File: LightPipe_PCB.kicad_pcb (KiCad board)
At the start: 4 copper layers, 38.8 x 38.8 mm, 14 parts, among them M1 2.2mm_M2, M2 2.2mm_M2, X1 KLB-4, X2 KLB-4, X3 XT30, X4.1 Cable-0.7mm, X4.2 Cable-0.7mm, X5.1 Cable-1.5mm, X5.2 Cable-1.5mm

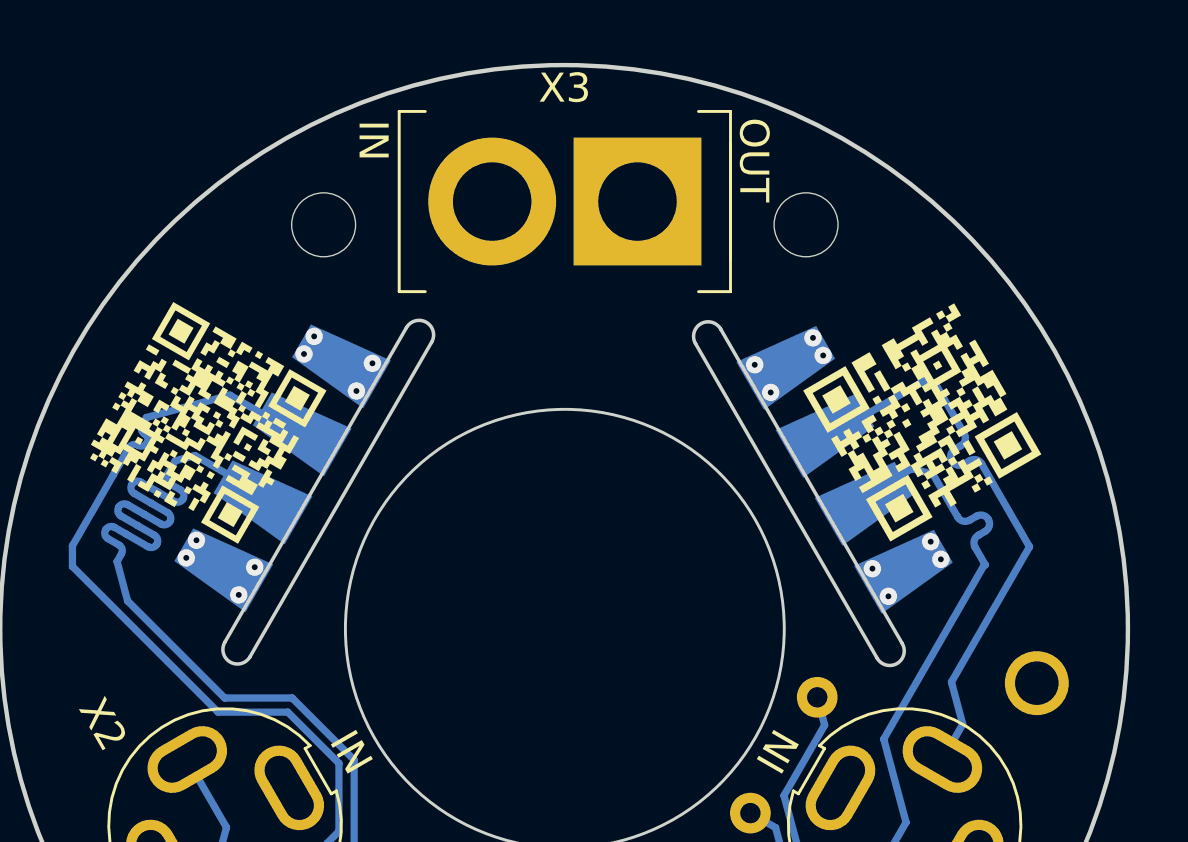
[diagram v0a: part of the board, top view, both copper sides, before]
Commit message: [clean] Optimized schematic to be easy readable as input PCB | changed 3D bodys in PCB to Input PCB positions | update date, company, project name and QR-code in schematic and board
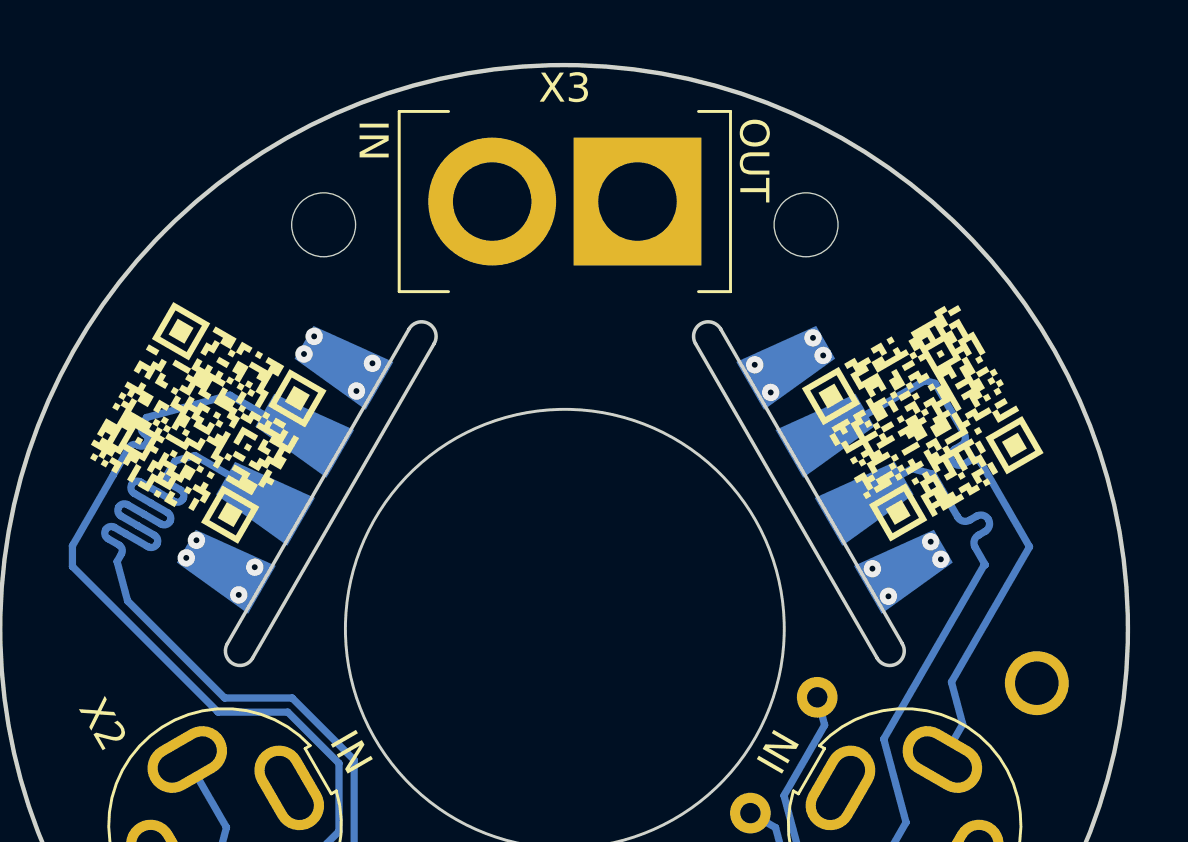
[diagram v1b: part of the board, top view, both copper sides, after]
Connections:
- LD1 pad 2: /clk2 -> /clk1
- LD1 pad 3: /d2 -> /d1
- LD2 pad 2: /clk1 -> /clk2
- LD2 pad 3: /d1 -> /d2
- LD3 pad 2: /clk1 -> /clk2
- LD3 pad 3: /d1 -> /d2
- X1 pad 1: /clk2 -> /clk1
- X1 pad 2: /d2 -> /d1
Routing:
- net /clk2: track 20.0 -> 45.5 mm
- net /clk1: track 45.5 -> 20.0 mm
- net /d2: track 20.0 -> 45.4 mm
- net /d1: track 45.4 -> 20.0 mm

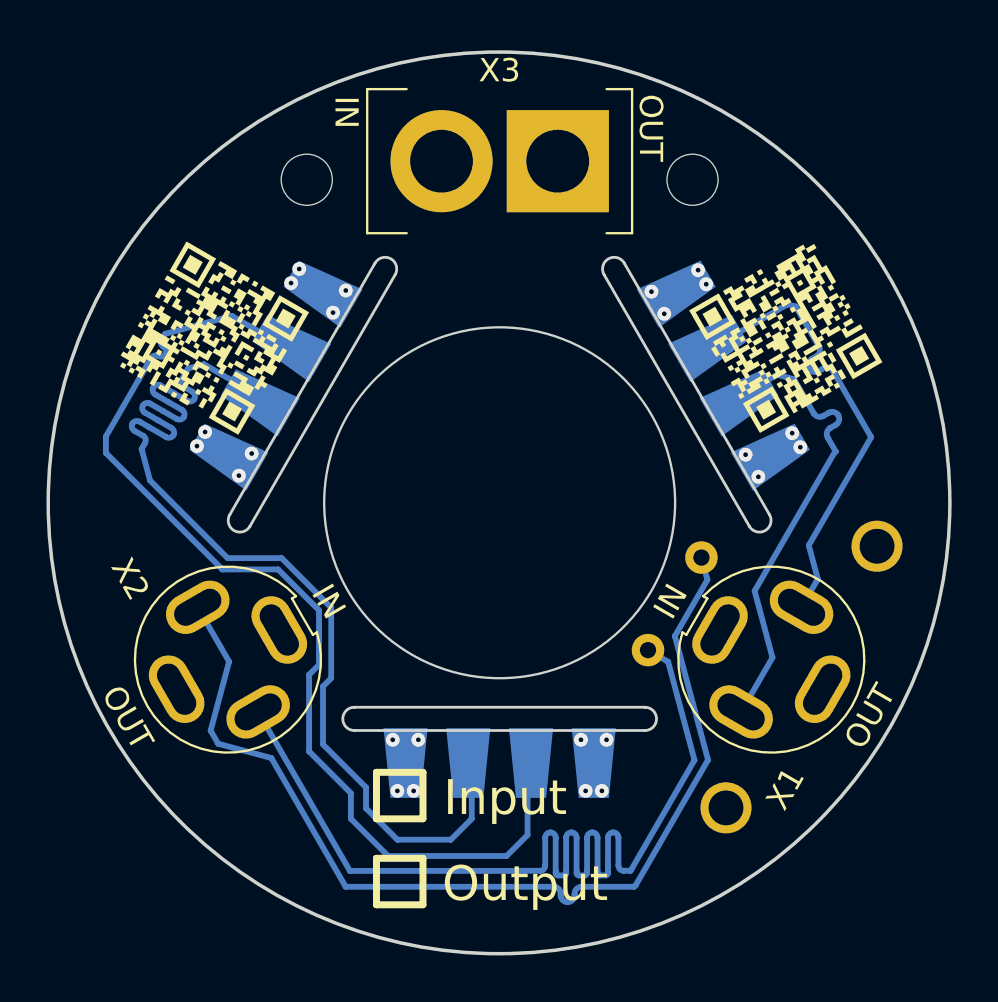
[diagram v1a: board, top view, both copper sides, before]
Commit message: [mechanical constrains] increased inner board diameter | reduced outer board diameter | added  PCB name, version and creator to silkscreen
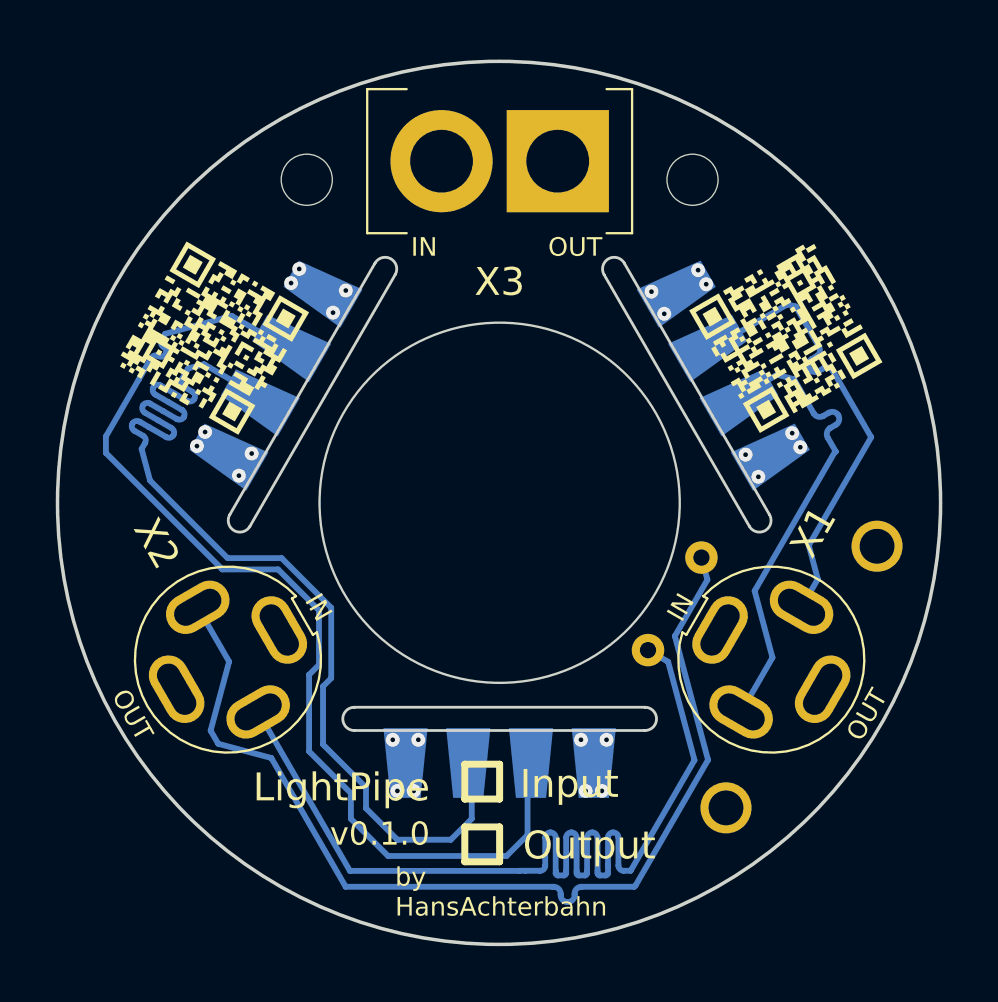
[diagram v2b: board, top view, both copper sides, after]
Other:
- board size 38.8 x 38.8 mm -> 38 x 38 mm
- board text added: "LightPipe"
- board text added: "by HansAchterbahn"
- board text added: "v0.1.0"

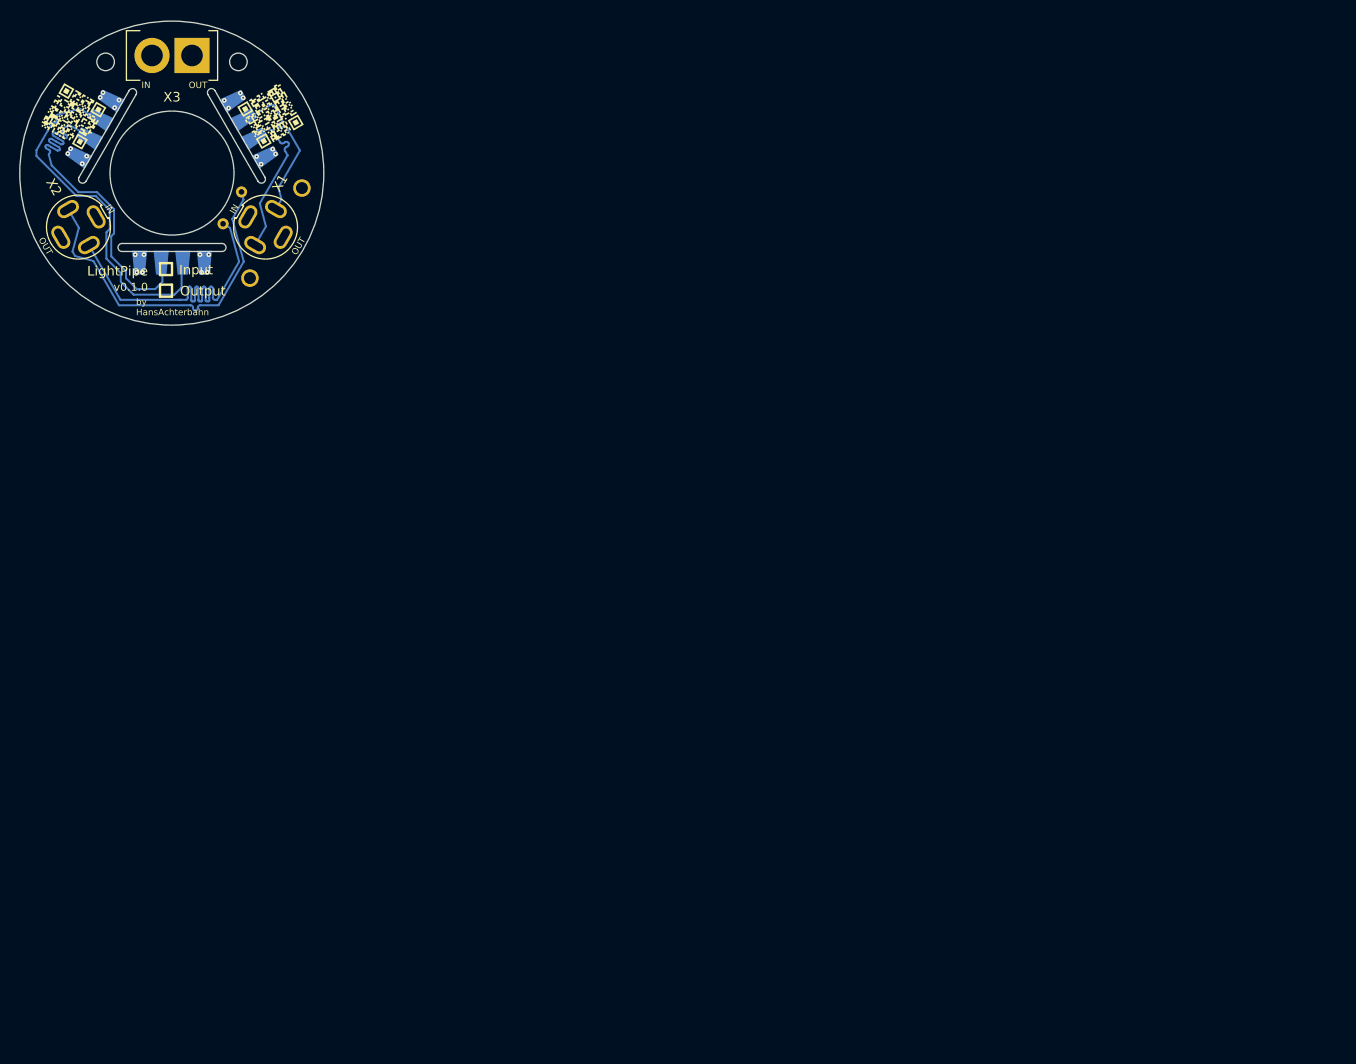
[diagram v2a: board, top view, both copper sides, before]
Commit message: [DRC] Solved DRC errors
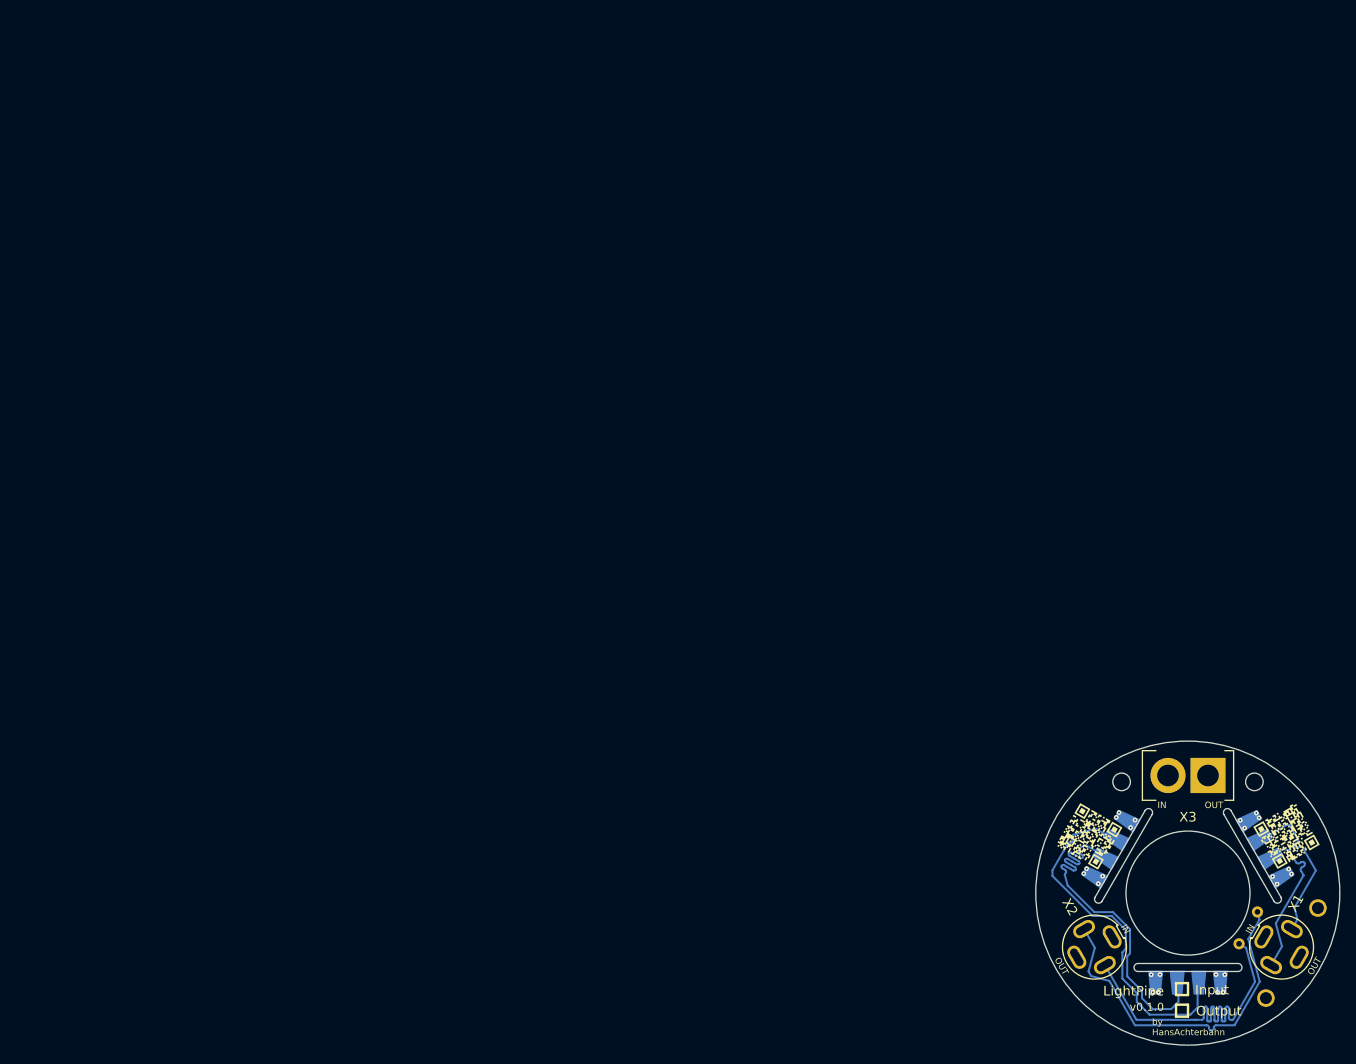
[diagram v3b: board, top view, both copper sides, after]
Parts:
- moved LD1 155.7 mm to (135.5, 85.1)
- moved LD2 155.7 mm to (118.5, 85.1)
- moved LD3 155.7 mm to (127.0, 99.8)
- moved M1 155.7 mm to (135.3, 76.1)
- moved M2 155.7 mm to (118.7, 76.1)
- moved QR1 155.7 mm to (139.3, 82.9)
- moved QR2 155.7 mm to (114.7, 82.9)
- moved X2 155.7 mm to (115.3, 96.8)
- moved X3 155.7 mm to (127.0, 75.3)
- moved X4.1 155.7 mm to (133.4, 96.3)
- moved X5.1 155.7 mm to (143.2, 91.9)
- moved X5.2 155.7 mm to (136.7, 103.1)
- moved X1 155.7 mm to (138.7, 96.8)
- moved X4.2 155.7 mm to (135.7, 92.4)

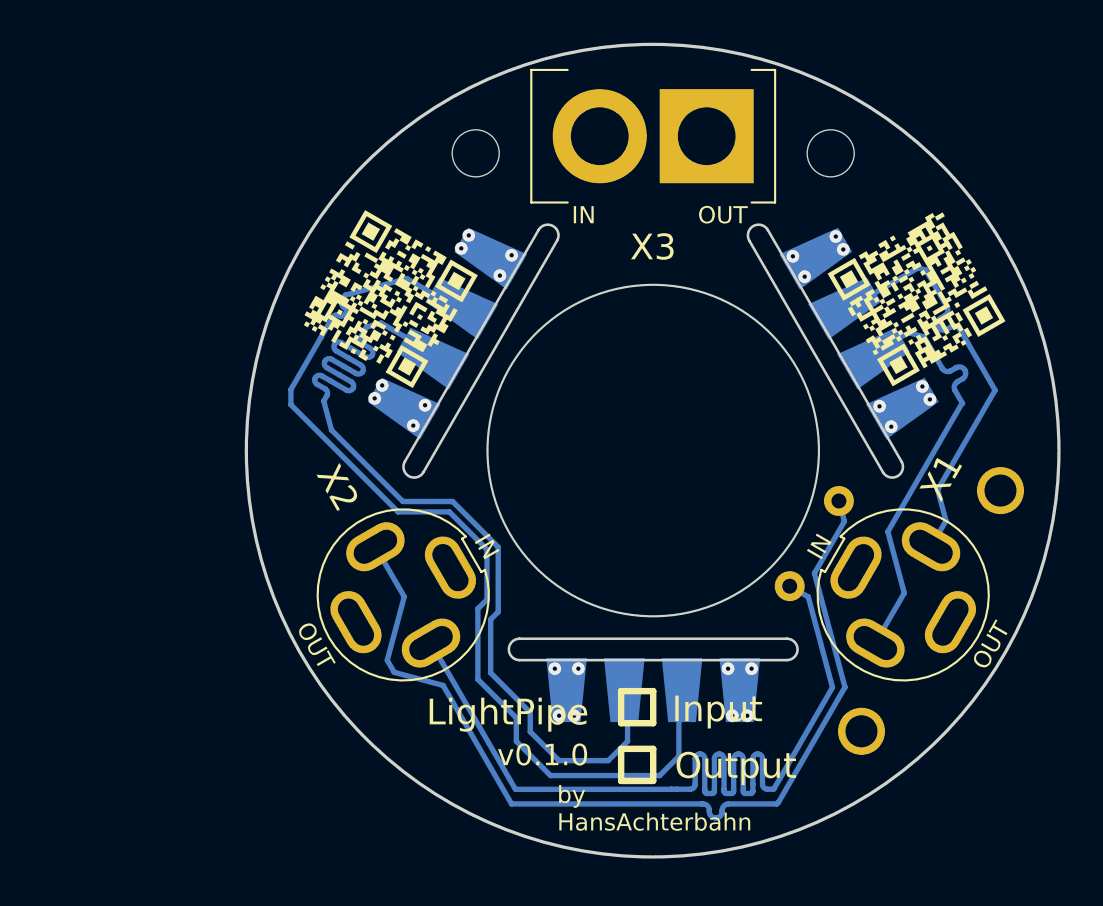
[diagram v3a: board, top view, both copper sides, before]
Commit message: [clean] improved schematic and pcb to be easier to read in Input-Mode
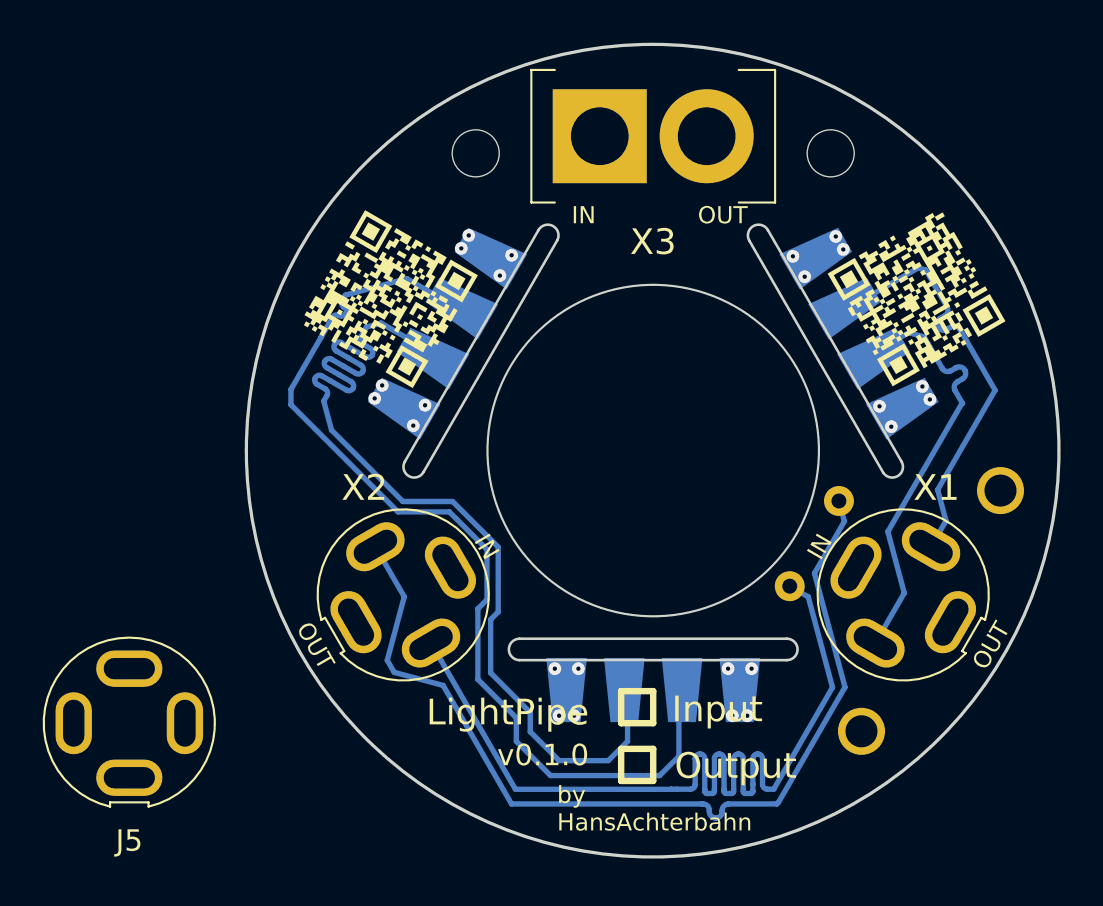
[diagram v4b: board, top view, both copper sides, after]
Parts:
- added J5: AudioJack4, h8-Connectors:Lumberg-KLB-4-Klinkensteckverbinder-3_5-180deg-turnable, F.Cu at (102.5, 102.8)
- turned X1 to 60 degrees
- turned X2 to -60 degrees
- turned X3 to 0 degrees
- renumbered X4.2 to X4.1, X4.1 to X4.2
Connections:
- X4.1 pad 1: /d3 -> /clk3
- X4.2 pad 1: /clk3 -> /d3
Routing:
- net /clk1: track 20.0 -> 0.00 mm
- net /d1: track 20.0 -> 39.9 mm
